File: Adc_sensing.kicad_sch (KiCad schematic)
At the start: 12 parts, among them U4 INA180A3, U5 MCP3204

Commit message: Commercial components selected
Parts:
- C20: footprint (none) -> Capacitor_SMD:C_0603_1608Metric_Pad1.08x0.95mm_HandSolder; Distributor Link (none) -> https://www.digikey.es/es/products/detail/kemet/C0603C104K5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
- D2, D3: Distributor Link (none) -> https://www.digikey.es/es/products/detail/diotec-semiconduc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
- NTC1: Distributor Link (none) -> https://www.digikey.es/es/products/detail/murata-electronic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
- R11, R12, R16: footprint Resistor_SMD:R_0603_1608Metric_Pad0.98x0.95mm_HandSolder -> Resistor_SMD:R_0805_2012Metric_Pad1.20x1.40mm_HandSolder; Distributor Link (none) -> https://www.digikey.es/es/products/detail/te-connectivity-p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
- R13, R15: Distributor Link (none) -> https://www.digikey.es/es/products/detail/yageo/RC0603FR-07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
- R14: Distributor Link (none) -> https://www.digikey.es/es/products/detail/stackpole-electro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
- U4: Distributor Link (none) -> https://www.digikey.es/es/products/detail/texas-instruments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
- U5: footprint (none) -> Package_SO:SOIC-14_3.9x8.7mm_P1.27mm; Distributor Link (none) -> https://www.digikey.es/es/products/detail/microchip-technol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
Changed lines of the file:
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@@
+			)
+		)
+		(property "Distributor Link" "https://www.digikey.es/es/products/detail/diotec-semiconductor/BZT52C3V3/13157359"
+			(at 246.38 128.27 90)
+			(effects
+				(font
+					(size 1.27 1.27)
+				)
+				(hide yes)
 			)
 		)
@@
 			)
 		)
+		(property "Distributor Link" "https://www.digikey.es/es/products/detail/texas-instruments/INA180A3IDBVR/8132988"
+			(at 226.06 71.12 0)
+			(effects
+				(font
+					(size 1.27 1.27)
+				)
+				(hide yes)
+			)
+		)
 		(pin "4"
 		)
@@
 			)
 		)
+		(property "Distributor Link" "https://www.digikey.es/es/products/detail/yageo/RC0603FR-0710KL/726880"
+			(at 46.99 74.93 0)
+			(effects
+				(font
+					(size 1.27 1.27)
+				)
+				(hide yes)
+			)
+		)
 		(pin "1"
 		)
@@
 			)
 		)
-		(property "Footprint" "Resistor_SMD:R_0603_1608Metric_Pad0.98x0.95mm_HandSolder"
+		(property "Footprint" "Resistor_SMD:R_0805_2012Metric_Pad1.20x1.40mm_HandSolder"
 			(at 82.042 58.42 90)
 			(effects
@@
 			)
 		)
+		(property "Distributor Link" "https://www.digikey.es/es/products/detail/te-connectivity-passive-product/CRG0805F39K/2380898"
+			(at 83.82 58.42 0)
+			(effects
+				(font
+					(size 1.27 1.27)
+				)
+				(hide yes)
+			)
+		)
 		(pin "1"
 		)
@@
 			)
 		)
+		(property "Distributor Link" "https://www.digikey.es/es/products/detail/diotec-semiconductor/BZT52C3V3/13157359"
+			(at 226.06 128.27 90)
+			(effects
+				(font
+					(size 1.27 1.27)
+				)
+				(hide yes)
+			)
+		)
 		(pin "1"
 		)
@@
 			)
 		)
-		(property "Footprint" "Resistor_SMD:R_0603_1608Metric_Pad0.98x0.95mm_HandSolder"
+		(property "Footprint" "Resistor_SMD:R_0805_2012Metric_Pad1.20x1.40mm_HandSolder"
 			(at 45.212 59.69 90)
 			(effects
@@
 			)
 		)
+		(property "Distributor Link" "https://www.digikey.es/es/products/detail/te-connectivity-passive-product/CRG0805F39K/2380898"
+			(at 46.99 59.69 0)
+			(effects
+				(font
+					(size 1.27 1.27)
+				)
+				(hide yes)
+			)
+		)
 		(pin "1"
 		)
@@
 			)
 		)
-		(property "Footprint" ""
+		(property "Footprint" "Package_SO:SOIC-14_3.9x8.7mm_P1.27mm"
 			(at 91.44 158.75 0)
 			(effects
@@
 			)
 		)
+		(property "Distributor Link" "https://www.digikey.es/es/products/detail/microchip-technology/MCP3204T-CI-SL/319441"
+			(at 68.58 151.13 0)
+			(effects
+				(font
+					(size 1.27 1.27)
+				)
+				(hide yes)
+			)
+		)
 		(pin "2"
 		)
@@
 			)
 		)
+		(property "Distributor Link" "https://www.digikey.es/es/products/detail/murata-electronics/NCP18XH103F03RB/1644665?s=N4IgTCBcDaIHIGEAKBGAHADQBIoAwGYAxAgJQCEQBdAXyA"
+			(at 153.67 78.74 0)
+			(effects
+				(font
+					(size 1.27 1.27)
+				)
+				(hide yes)
+			)
+		)
 		(pin "1"
 		)
@@
 			)
 		)
+		(property "Distributor Link" "https://www.digikey.es/es/products/detail/yageo/RC0603FR-0710KL/726880"
+			(at 153.67 64.77 0)
+			(effects
+				(font
+					(size 1.27 1.27)
+				)
+				(hide yes)
+			)
+		)
 		(pin "1"
 		)
@@
 			)
 		)
+		(property "Distributor Link" "https://www.digikey.es/es/products/detail/stackpole-electronics-inc/RMCF0603FT1K00/1761077"
+			(at 241.3 71.12 90)
+			(effects
+				(font
+					(size 1.27 1.27)
+				)
+				(hide yes)
+			)
+		)
 		(pin "1"
 		)
@@
 			)
 		)
-		(property "Footprint" ""
+		(property "Footprint" "Capacitor_SMD:C_0603_1608Metric_Pad1.08x0.95mm_HandSolder"
 			(at 252.4252 80.01 0)
 			(effects
@@
 			)
 		)
+		(property "Distributor Link" "https://www.digikey.es/es/products/detail/kemet/C0603C104K5RACTU/1465594"
+			(at 251.46 76.2 0)
+			(effects
+				(font
+					(size 1.27 1.27)
+				)
+				(hide yes)
+			)
+		)
 		(pin "1"
 		)
@@
 			)
 		)
-		(property "Footprint" "Resistor_SMD:R_0603_1608Metric_Pad0.98x0.95mm_HandSolder"
+		(property "Footprint" "Resistor_SMD:R_0805_2012Metric_Pad1.20x1.40mm_HandSolder"
 			(at 82.042 76.2 90)
 			(effects
@@
 			(at 83.82 76.2 0)
 			(effects
+				(font
+					(size 1.27 1.27)
+				)
+				(hide yes)
+			)
+		)
+		(property "Distributor Link" "https://www.digikey.es/es/products/detail/te-connectivity-passive-product/CRG0805F39K/2380898"
+			(at 83.82 76.2 0)
+			(effects

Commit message: over-voltage protection added
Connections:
- net +3V3: no longer D2.1 (K), D3.1 (K), R11.1, R11.2, R16.1, U5.2 (CH1)
- net VIN_SENSING: now also D3.1 (K); no longer R12.1
- net V_SHUNT_MINUS renamed VSHUNT_MINUS
- net V_SHUNT_PLUS renamed VSHUNT_PLUS
- new net VIN: R12.1
- new net VOUT: R11.1
- new net VOUT_SENSING: D2.1 (K), R11.2, R16.1, U5.2 (CH1)

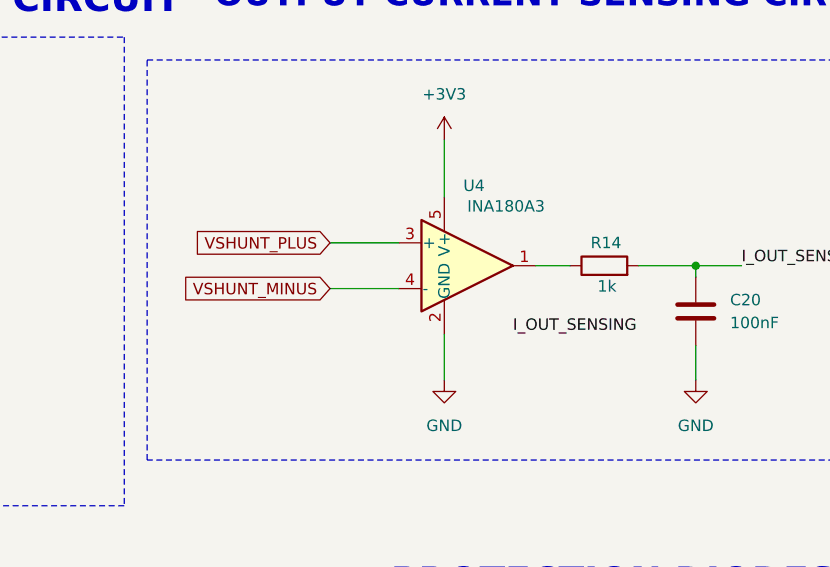
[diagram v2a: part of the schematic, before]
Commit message: Placement finished routing started
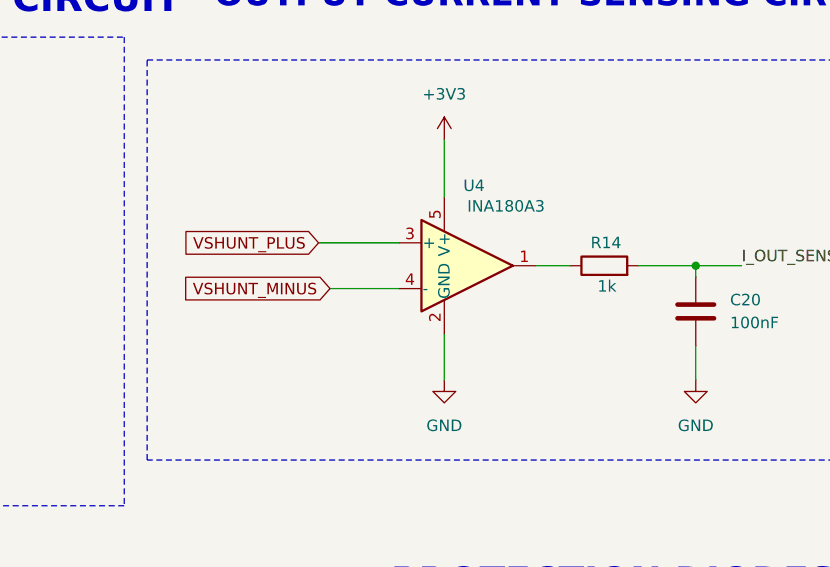
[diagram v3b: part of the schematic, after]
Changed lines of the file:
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@@
 	(wire
 		(pts
-			(xy 210.82 68.58) (xy 218.44 68.58)
+			(xy 209.55 68.58) (xy 218.44 68.58)
 		)
 		(stroke
@@
 	(label "I_OUT_SENSING"
 		(at 38.1 153.67 0)
-		(effects
-			(font
-				(size 1.27 1.27)
-			)
-			(justify left bottom)
-		)
-	)
-	(label "I_OUT_SENSING"
-		(at 231.14 78.74 0)
 		(effects
 			(font
@@
 	(global_label "VSHUNT_PLUS"
 		(shape input)
-		(at 210.82 68.58 180)
+		(at 209.55 68.58 180)
 		(fields_autoplaced yes)
 		(effects
@@
 		)
 		(property "Intersheetrefs" "${INTERSHEET_REFS}"
-			(at 194.7719 68.58 0)
+			(at 193.5019 68.58 0)
 			(effects
 				(font
